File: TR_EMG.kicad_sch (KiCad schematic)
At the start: 0 parts

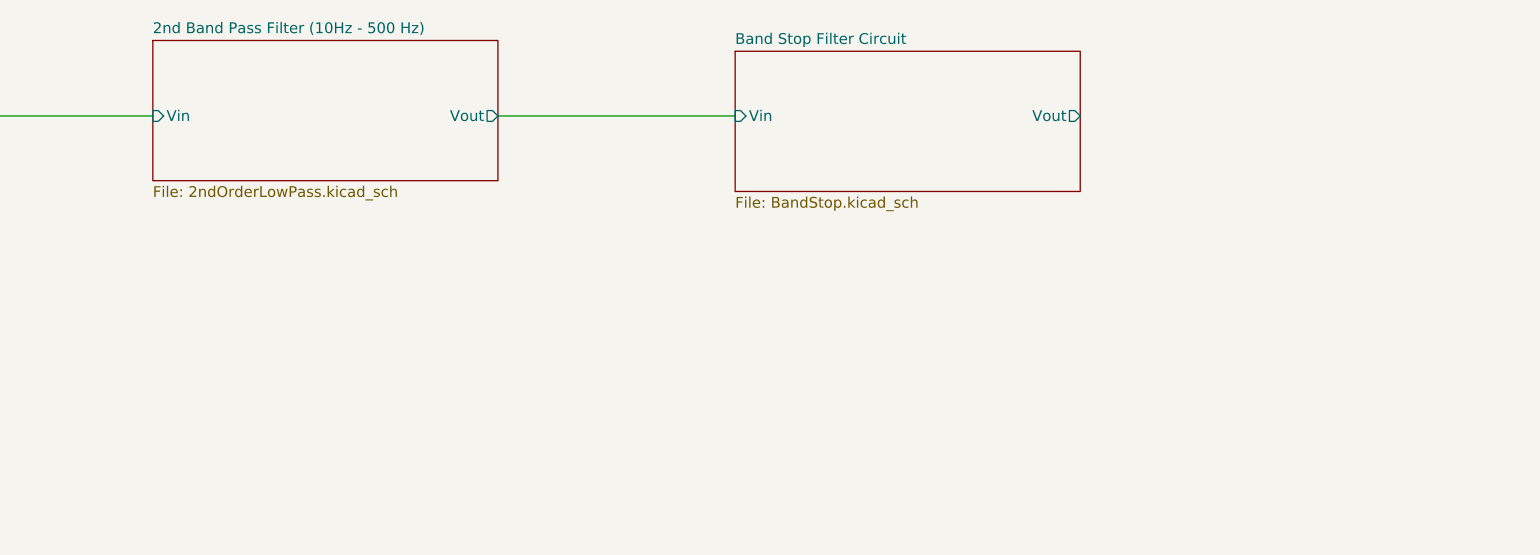
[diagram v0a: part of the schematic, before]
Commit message: add ADC block
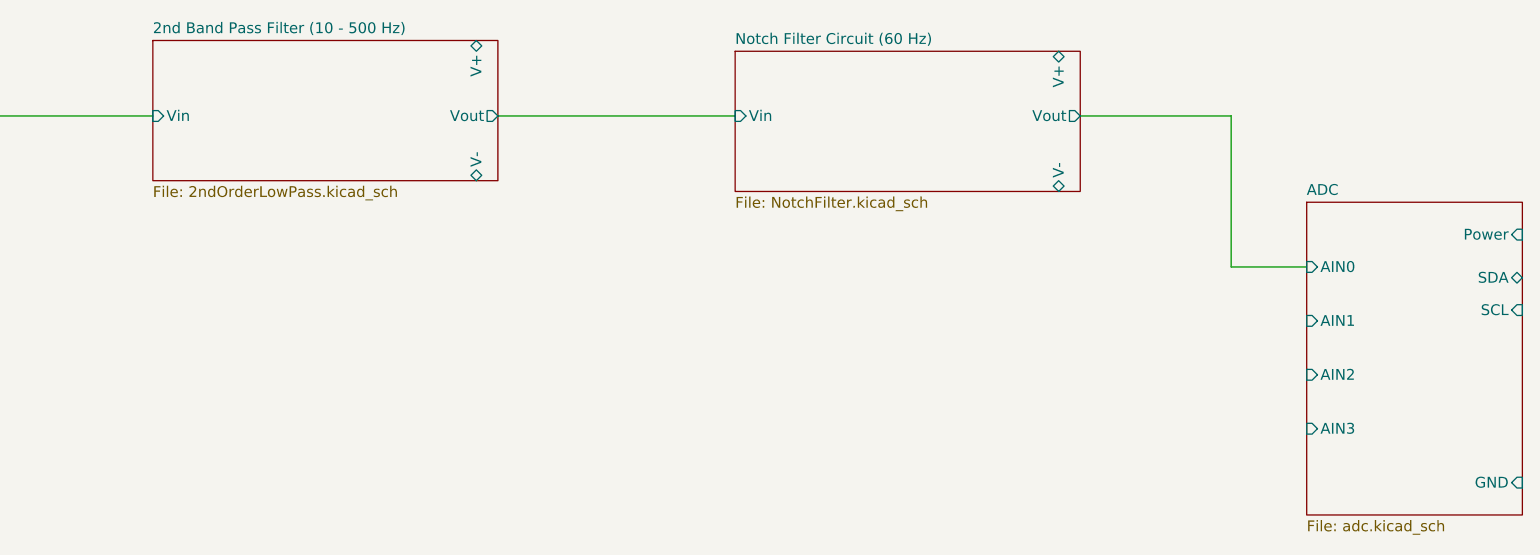
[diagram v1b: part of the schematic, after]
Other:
- sheet 2nd Band Pass Filter (10Hz - 500 Hz) renamed 2nd Band Pass Filter (10 - 500 Hz)
- sheet Band Stop Filter Circuit renamed Notch Filter Circuit (60 Hz)
- added sheet ADC (adc.kicad_sch)
- sheet 2nd Band Pass Filter (10 - 500 Hz) ports: added V+, V-; removed none
- sheet Notch Filter Circuit (60 Hz): file BandStop.kicad_sch -> NotchFilter.kicad_sch
- sheet Notch Filter Circuit (60 Hz) ports: added V+, V-; removed none
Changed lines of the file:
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@@
     (company "Northeastern University")
   )
+  (wire (pts (xy 228.6 46.99) (xy 228.6 64.77))
+    (stroke (width 0) (type default))
+  )
   (wire (pts (xy 82.55 46.99) (xy 101.6 46.99))
+    (stroke (width 0) (type default))
+  )
+  (wire (pts (xy 210.82 46.99) (xy 228.6 46.99))
+    (stroke (width 0) (type default))
+  )
+  (wire (pts (xy 228.6 64.77) (xy 237.49 64.77))
     (stroke (width 0) (type default))
   )
@@
     (stroke (width 0.1524) (type solid))
     (fill (color 0 0 0 0.0000))
-    (property "Sheetname" "2nd Band Pass Filter (10Hz - 500 Hz)" (at 101.6 37.3884 0)
+    (property "Sheetname" "2nd Band Pass Filter (10 - 500 Hz)" (at 101.6 37.3884 0)
       (effects (font (size 1.27 1.27)) (justify left bottom))
     )
@@
       (effects (font (size 1.27 1.27)) (justify left))
     )
+    (pin "V-" bidirectional (at 139.7 54.61 270)
+      (effects (font (size 1.27 1.27)) (justify left))
+    )
+    (pin "V+" bidirectional (at 139.7 38.1 90)
+      (effects (font (size 1.27 1.27)) (justify right))
+    )
     (instances
       (project "TR_EMG"
@@
     (stroke (width 0.1524) (type solid))
     (fill (color 0 0 0 0.0000))
-    (property "Sheetname" "Band Stop Filter Circuit" (at 170.18 38.6584 0)
+    (property "Sheetname" "Notch Filter Circuit (60 Hz)" (at 170.18 38.6584 0)
       (effects (font (size 1.27 1.27)) (justify left bottom))
     )
-    (property "Sheetfile" "BandStop.kicad_sch" (at 170.18 56.4646 0)
+    (property "Sheetfile" "NotchFilter.kicad_sch" (at 170.18 56.4646 0)
       (effects (font (size 1.27 1.27)) (justify left top))
     )
@@
       (effects (font (size 1.27 1.27)) (justify left))
     )
+    (pin "V-" bidirectional (at 208.28 55.88 270)
+      (effects (font (size 1.27 1.27)) (justify left))
+    )
+    (pin "V+" bidirectional (at 208.28 39.37 90)
+      (effects (font (size 1.27 1.27)) (justify right))
+    )
     (instances
       (project "TR_EMG"
@@
       )
     )
+  )
+  (sheet (at 237.49 57.15) (size 25.4 36.83) (fields_autoplaced)
+    (stroke (width 0.1524) (type solid))
+    (fill (color 0 0 0 0.0000))
+    (property "Sheetname" "ADC" (at 237.49 56.4384 0) (show_name)
+      (effects (font (size 1.27 1.27)) (justify left bottom))
+    )
+    (property "Sheetfile" "adc.kicad_sch" (at 237.49 94.5646 0)
+      (effects (font (size 1.27 1.27)) (justify left top))
+    )
+    (pin "AIN3" input (at 237.49 83.82 180)
+      (effects (font (size 1.27 1.27)) (justify left))
+    )
+    (pin "AIN1" input (at 237.49 71.12 180)
+      (effects (font (size 1.27 1.27)) (justify left))
+    )
+    (pin "AIN2" input (at 237.49 77.47 180)
+      (effects (font (size 1.27 1.27)) (justify left))
+    )
+    (pin "SDA" bidirectional (at 262.89 66.04 0)
+      (effects (font (size 1.27 1.27)) (justify right))
+    )
+    (pin "SCL" input (at 262.89 69.85 0)
+      (effects (font (size 1.27 1.27)) (justify right))
+    )
+    (pin "Power" input (at 262.89 60.96 0)
+      (effects (font (size 1.27 1.27)) (justify right))
+    )
+    (pin "GND" input (at 262.89 90.17 0)
+      (effects (font (size 1.27 1.27)) (justify right))
+    )
+    (pin "AIN0" input (at 237.49 64.77 180)
+      (effects (font (size 1.27 1.27)) (justify left))
+    )
+    (instances
+      (project "TR_EMG"
+        (path "/c6167f6f-8a8c-40a1-9c06-7f0e8ea44639" (page "5"))
+      )
+    )

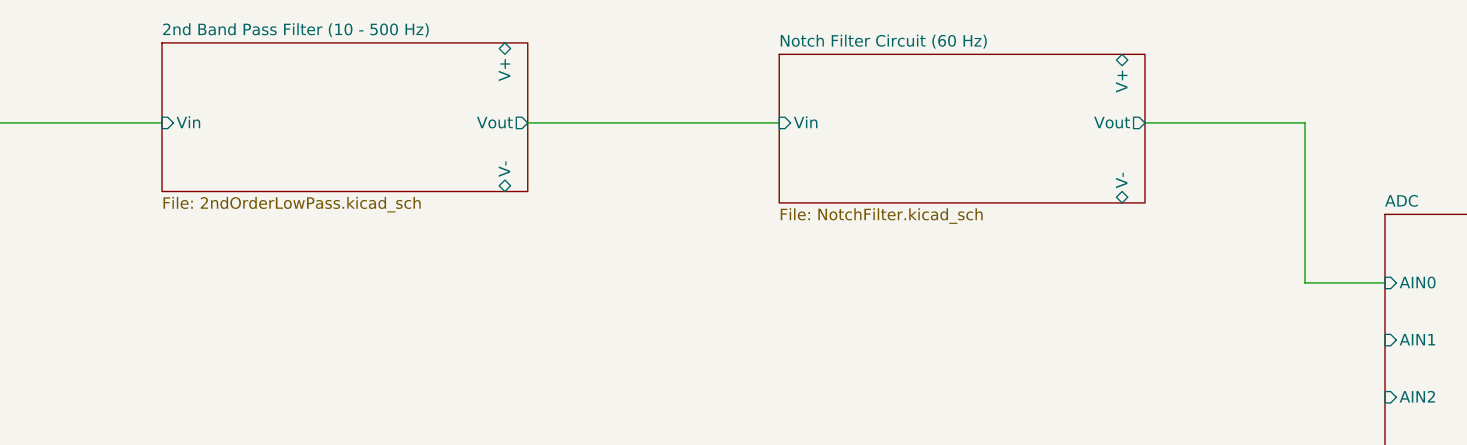
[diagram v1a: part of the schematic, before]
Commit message: swapped lpf and hpf in bandpass filter and added testpoints on various filter circuits
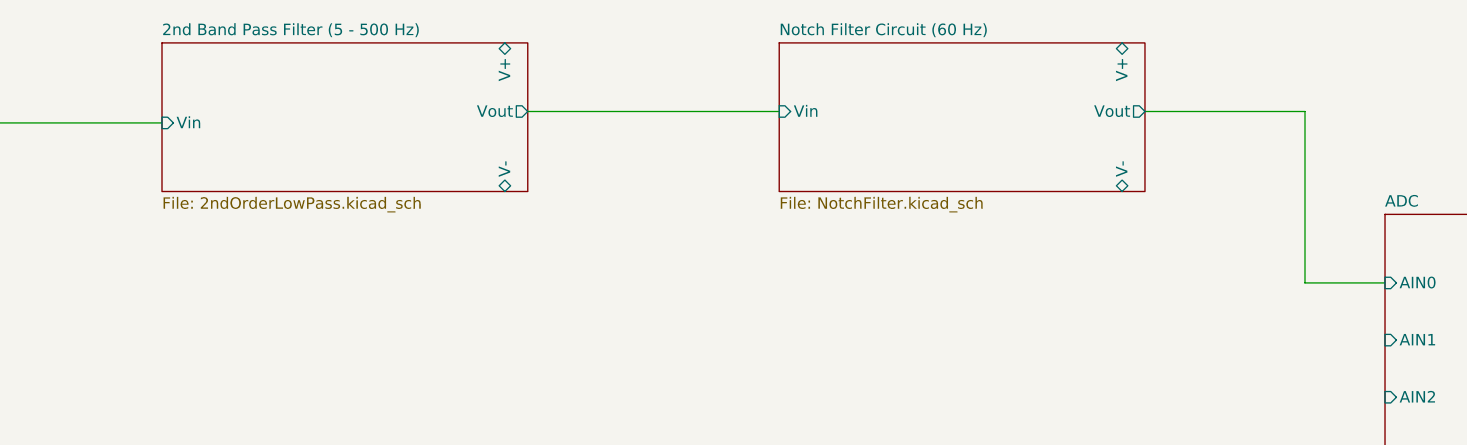
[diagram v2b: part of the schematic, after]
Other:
- sheet 2nd Band Pass Filter (10 - 500 Hz) renamed 2nd Band Pass Filter (5 - 500 Hz)
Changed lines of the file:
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@@
     (company "Northeastern University")
   )
-  (wire (pts (xy 228.6 46.99) (xy 228.6 64.77))
+  (wire (pts (xy 228.6 45.72) (xy 228.6 64.77))
     (stroke (width 0) (type default))
   )
@@
     (stroke (width 0) (type default))
   )
-  (wire (pts (xy 210.82 46.99) (xy 228.6 46.99))
+  (wire (pts (xy 210.82 45.72) (xy 228.6 45.72))
     (stroke (width 0) (type default))
   )
@@
     (stroke (width 0) (type default))
   )
-  (wire (pts (xy 142.24 46.99) (xy 170.18 46.99))
+  (wire (pts (xy 142.24 45.72) (xy 170.18 45.72))
     (stroke (width 0) (type default))
   )
@@
     (stroke (width 0.1524) (type solid))
     (fill (color 0 0 0 0.0000))
-    (property "Sheetname" "2nd Band Pass Filter (10 - 500 Hz)" (at 101.6 37.3884 0)
+    (property "Sheetname" "2nd Band Pass Filter (5 - 500 Hz)" (at 101.6 37.3884 0)
       (effects (font (size 1.27 1.27)) (justify left bottom))
     )
@@
       (effects (font (size 1.27 1.27)) (justify left top))
     )
-    (pin "Vout" output (at 142.24 46.99 0)
+    (pin "Vout" output (at 142.24 45.72 0)
       (effects (font (size 1.27 1.27)) (justify right))
     )
@@
     )
   )
-  (sheet (at 170.18 39.37) (size 40.64 16.51) (fields_autoplaced)
+  (sheet (at 170.18 38.1) (size 40.64 16.51) (fields_autoplaced)
     (stroke (width 0.1524) (type solid))
     (fill (color 0 0 0 0.0000))
-    (property "Sheetname" "Notch Filter Circuit (60 Hz)" (at 170.18 38.6584 0)
+    (property "Sheetname" "Notch Filter Circuit (60 Hz)" (at 170.18 37.3884 0)
       (effects (font (size 1.27 1.27)) (justify left bottom))
     )
-    (property "Sheetfile" "NotchFilter.kicad_sch" (at 170.18 56.4646 0)
+    (property "Sheetfile" "NotchFilter.kicad_sch" (at 170.18 55.1946 0)
       (effects (font (size 1.27 1.27)) (justify left top))
     )
-    (pin "Vout" output (at 210.82 46.99 0)
+    (pin "Vout" output (at 210.82 45.72 0)
       (effects (font (size 1.27 1.27)) (justify right))
     )
-    (pin "Vin" input (at 170.18 46.99 180)
+    (pin "Vin" input (at 170.18 45.72 180)
       (effects (font (size 1.27 1.27)) (justify left))
     )
-    (pin "V-" bidirectional (at 208.28 55.88 270)
+    (pin "V-" bidirectional (at 208.28 54.61 270)
       (effects (font (size 1.27 1.27)) (justify left))
     )
-    (pin "V+" bidirectional (at 208.28 39.37 90)
+    (pin "V+" bidirectional (at 208.28 38.1 90)
       (effects (font (size 1.27 1.27)) (justify right))
     )

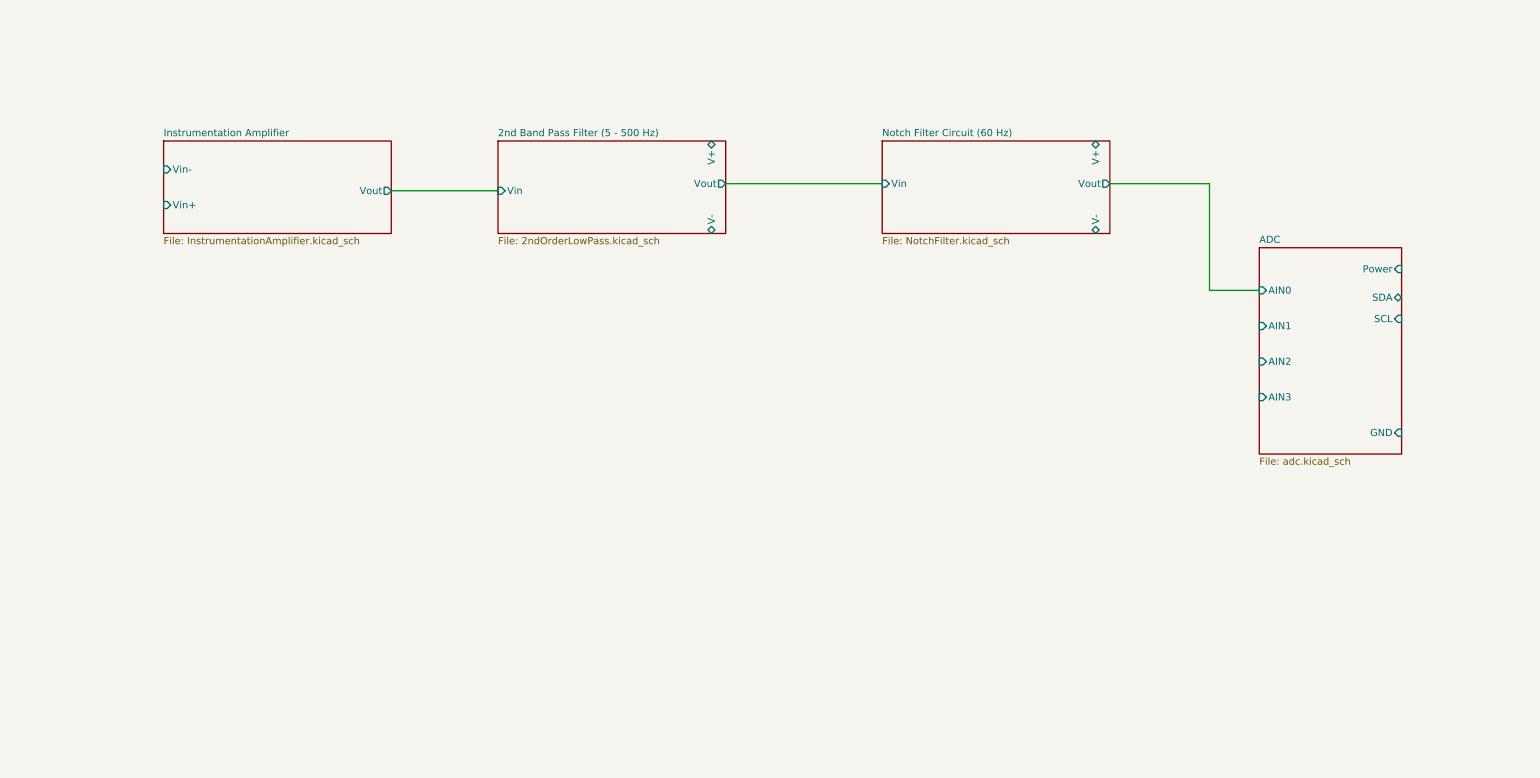
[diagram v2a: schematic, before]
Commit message: Filter abstraction and Input output connectors
Abstracted filters so there are 4 signal paths to go to ADC. Added input and output connectors.
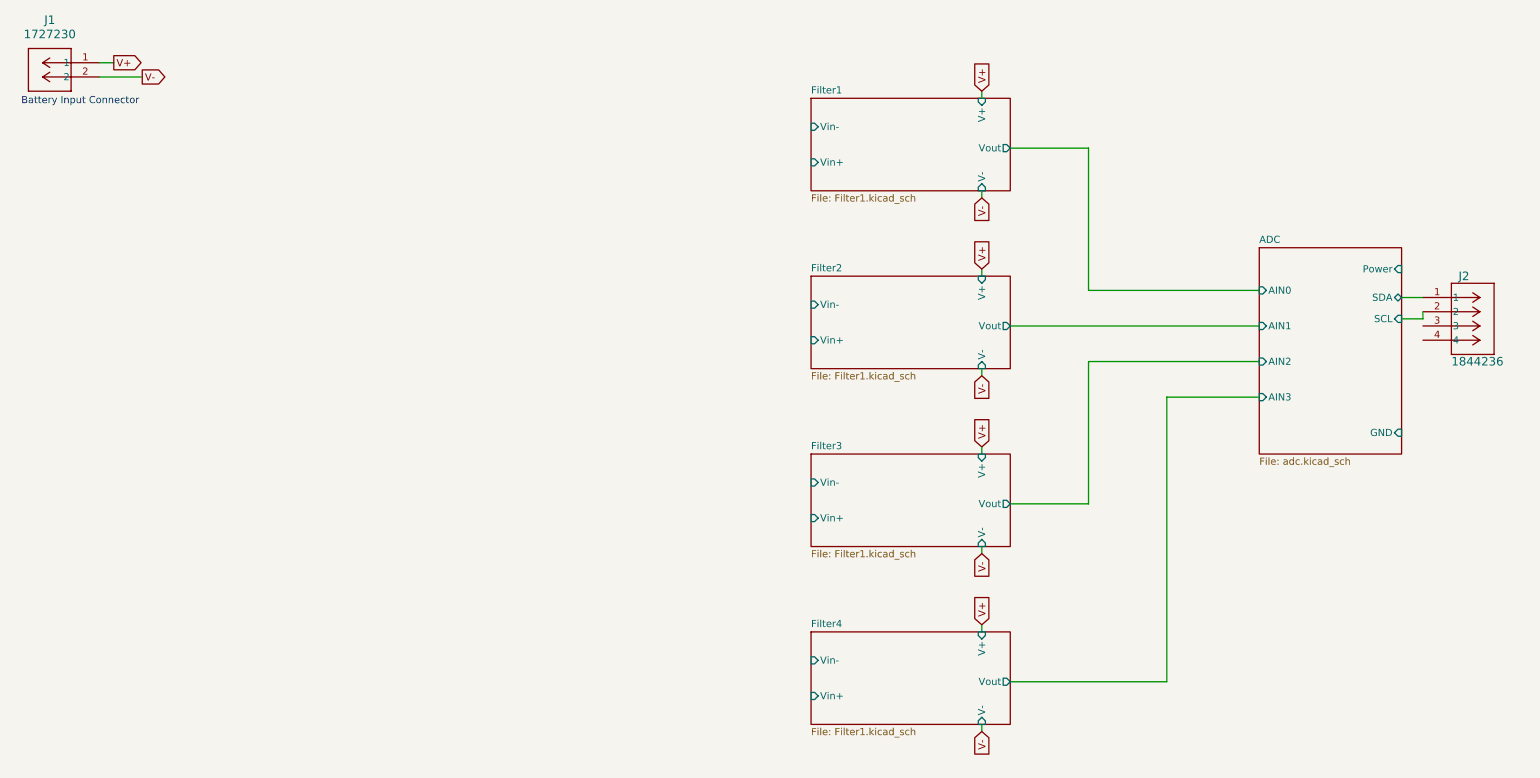
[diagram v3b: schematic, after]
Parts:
- added J1: 1727230, CONN_1727230_PXC, symbol 1727230:1727230
- added J2: 1844236, CONN_1844236_PXC, symbol 1844236:1844236
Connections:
- net ADC/SCL: now also J2.2
- net ADC/SDA: now also J2.1
- new net V+: J1.1
- new net V-: J1.2
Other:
- removed sheet 2nd Band Pass Filter (5 - 500 Hz)
- removed sheet Instrumentation Amplifier
- removed sheet Notch Filter Circuit (60 Hz)
- added sheet Filter1 (Filter1.kicad_sch)
- added sheet Filter2 (Filter1.kicad_sch)
- added sheet Filter3 (Filter1.kicad_sch)
- added sheet Filter4 (Filter1.kicad_sch)
- note added: "Battery Input Connector"

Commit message: added connectors for electrode inputs and revamped battery connectors
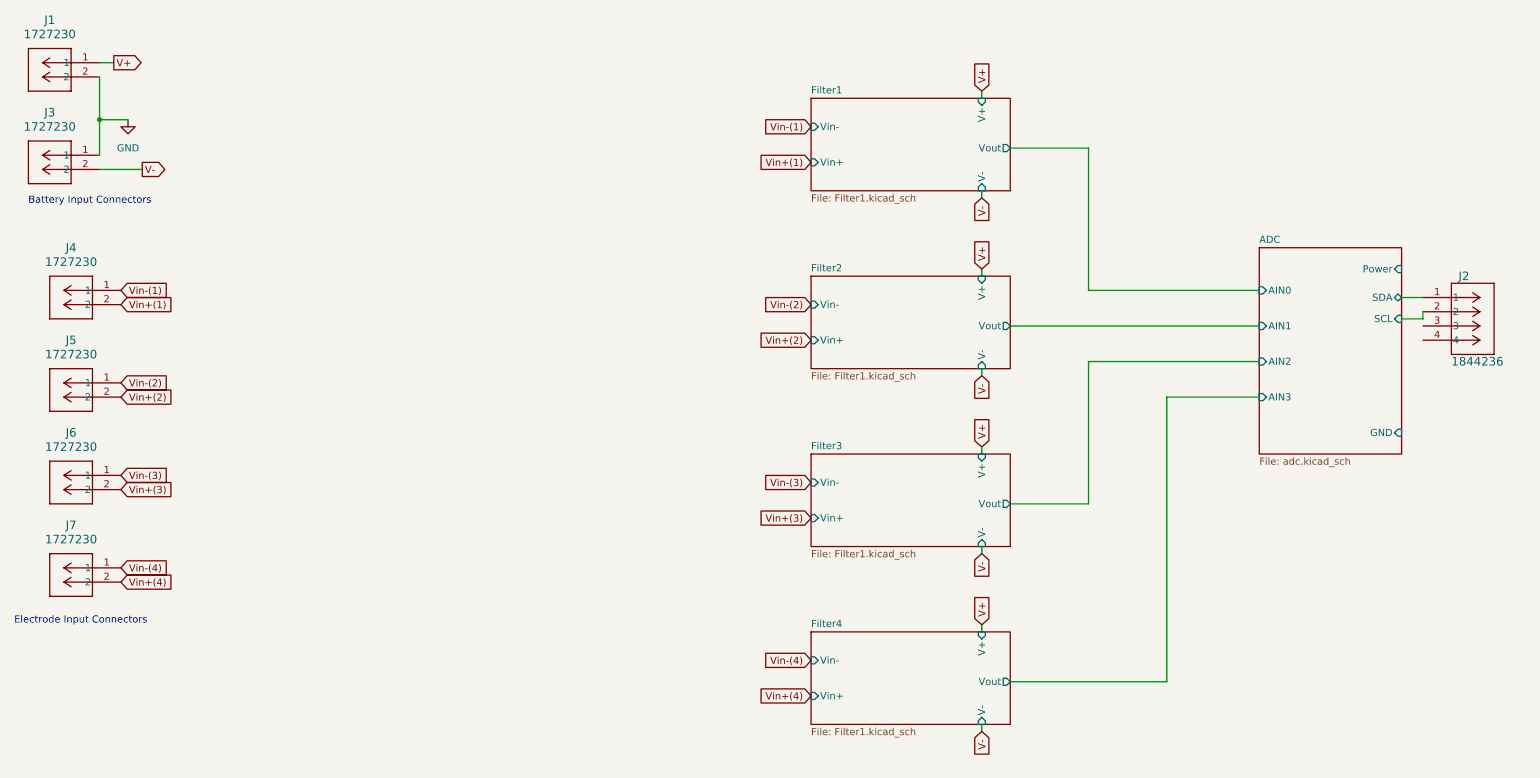
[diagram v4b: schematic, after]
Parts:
- added J3, J4, J5, J6, J7: 1727230, CONN_1727230_PXC, symbol 1727230:1727230
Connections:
- net V-: now also J3.2; no longer J1.2
- new net GND: J1.2, J3.1
- new net Vin+(1): J4.2
- new net Vin+(2): J5.2
- new net Vin+(3): J6.2
- new net Vin+(4): J7.2
- new net Vin-(1): J4.1
- new net Vin-(2): J5.1
- new net Vin-(3): J6.1
- new net Vin-(4): J7.1
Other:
- note added: "Battery Input Connectors"
- note added: "Electrode Input Connectors"
- note removed: "Battery Input Connector"
